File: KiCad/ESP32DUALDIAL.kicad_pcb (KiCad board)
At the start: 2 copper layers, 180.5 x 74 mm, 80 parts, among them J1 SERVICE, J2 Conn_01x04_Male, J3 mode, J5 Conn_01x03_Male, J6 Conn_01x02_Male, J7 Conn_01x02_Male, J8 Conn_01x02_Male, M1 Fan_CPU_4pin, M2 Fan_CPU_4pin, Q1 Q_NMOS_GDS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

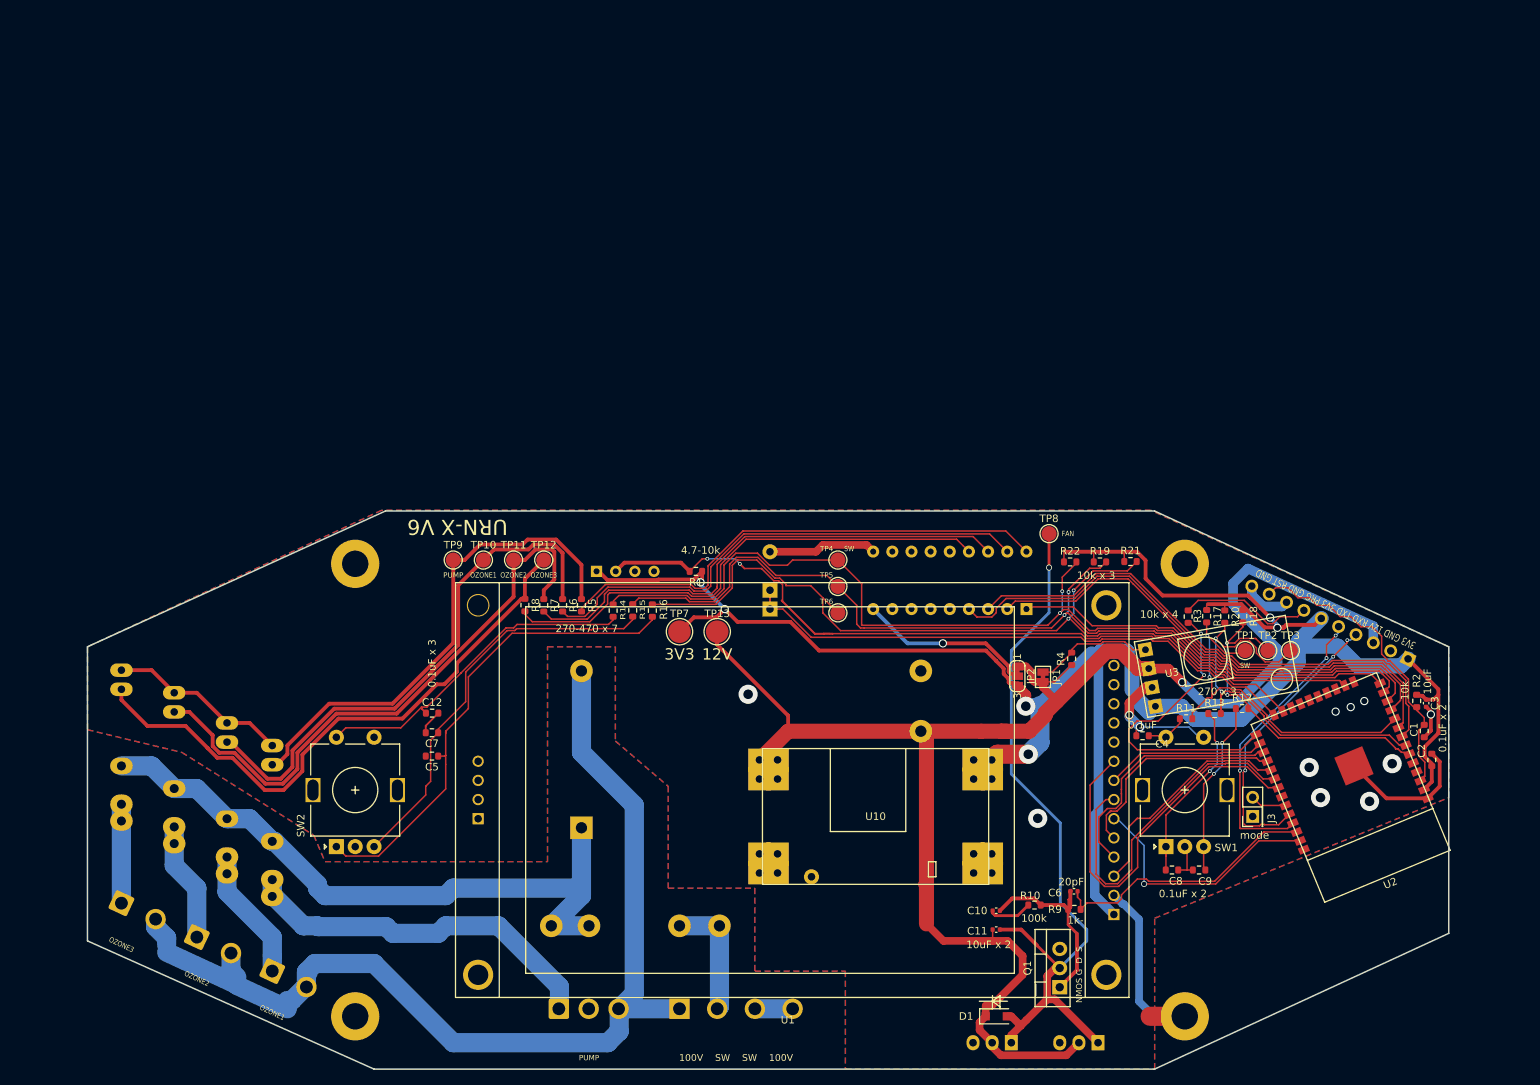
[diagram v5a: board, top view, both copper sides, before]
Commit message: Version6 release. Testpad add and follow more SSR type.
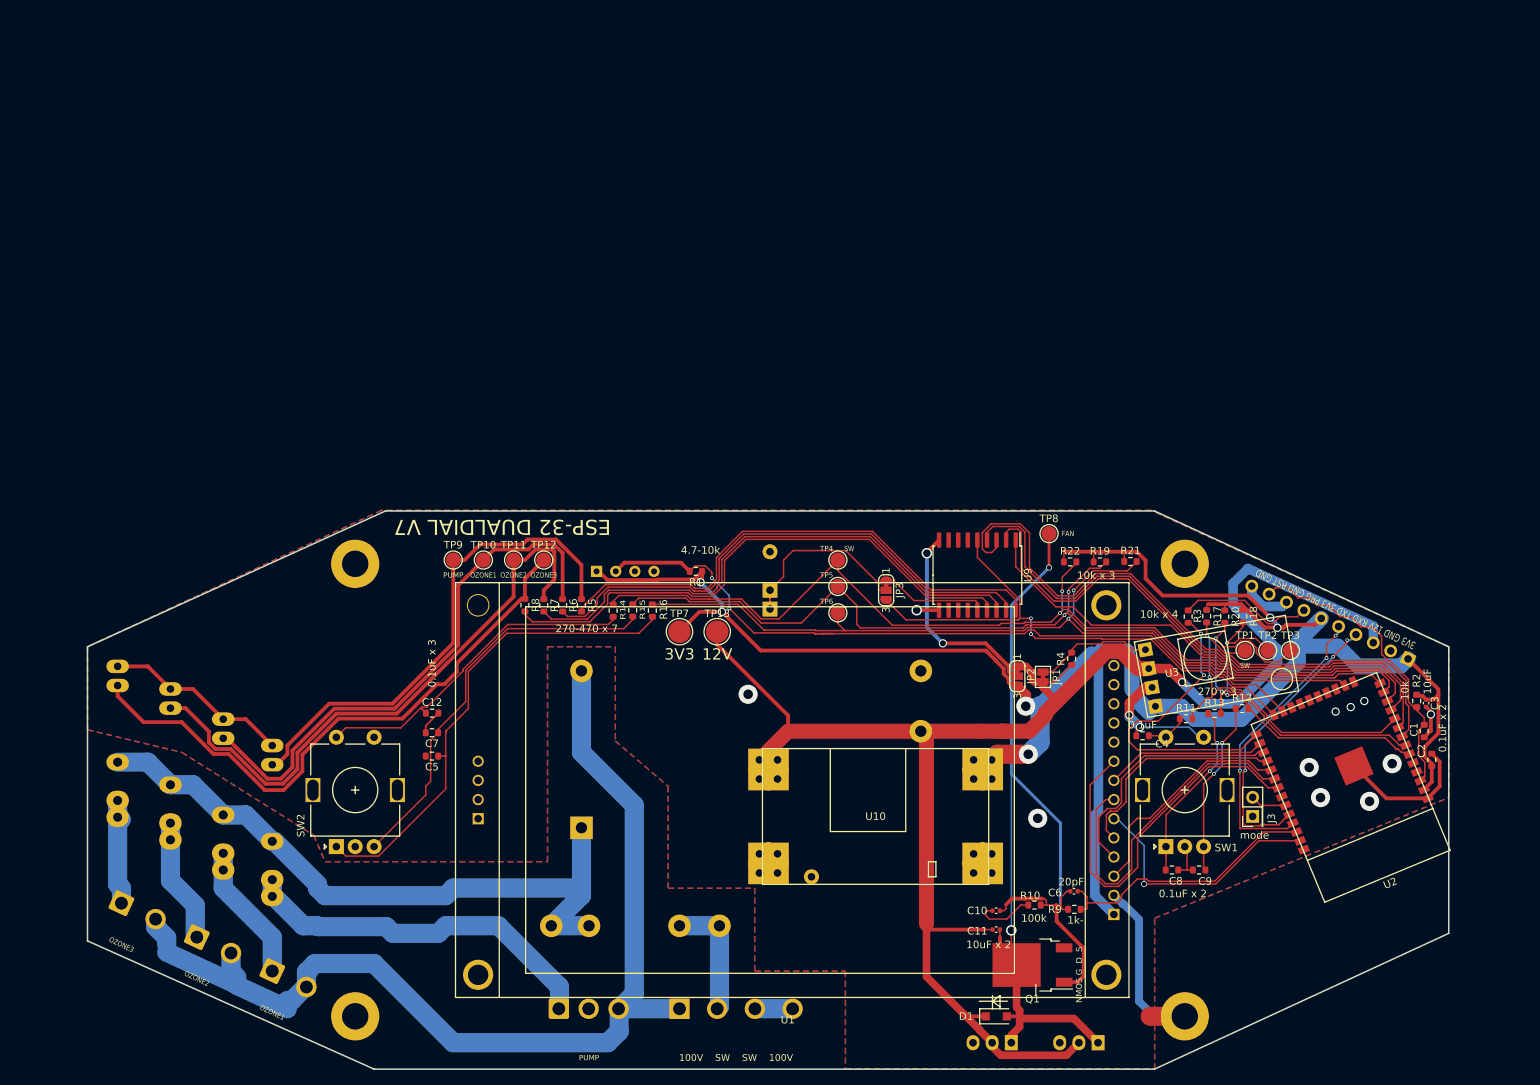
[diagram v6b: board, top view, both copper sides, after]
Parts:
- added JP3: Jumper_NC_Dual, Jumper:SolderJumper-3_P1.3mm_Bridged12_RoundedPad1.0x1.5mm_NumberLabels, F.Cu at (130.4, 83.5)
- Q1: footprint Package_TO_SOT_THT:TO-220-3_Vertical -> Package_TO_SOT_SMD:TO-252-2
- U9: footprint Package_DIP:DIP-18_W7.62mm -> Package_SO:SOIC-18W_7.5x11.6mm_P1.27mm; moved to F.Cu
- moved U9 7.91 mm to (142.5, 81.5), turned to 270 degrees
- moved Q1 4.66 mm to (149.8, 133.2), turned to 180 degrees
- moved U6 0.71 mm to (42.5, 109.5)
- moved U7 0.71 mm to (35.5, 105.5)
- moved U8 0.71 mm to (28.5, 102.5)
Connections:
- U2 pad 24: Net-(BZ1-Pad1) -> BUZZER
- U9 pad 5: Net-(U9-Pad5) -> BUZZER
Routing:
- net BUZZER: track 0.00 -> 72.1 mm, vias 0 -> 2
- net Net-(BZ1-Pad1): track 76.8 -> 25.5 mm
- net Net-(JP3-Pad1): track 0.00 -> 14.3 mm
- net OZON1: track 71.6 -> 84.3 mm
- net Net-(C11-Pad1): track 100.4 -> 108.9 mm, vias 1 -> 2
- net GND: track 128.6 -> 120.1 mm, vias 12 -> 13
- net Net-(R16-Pad2): track 122.5 -> 114.3 mm
- net OZON0: track 63.9 -> 71.6 mm
- net PUMP: track 56.5 -> 63.5 mm
- net Net-(R1-Pad2): track 108.8 -> 101.9 mm
- net Net-(R8-Pad2): track 67.8 -> 74.0 mm
- net Net-(R7-Pad2): track 67.6 -> 73.1 mm
- net Net-(JP2-Pad2): track 23.8 -> 27.9 mm, vias 1 -> 2
- net Net-(R6-Pad2): track 67.2 -> 71.0 mm
- net OZON2: track 73.0 -> 76.8 mm
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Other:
- board text added: "ESP-32 DUALDIAL V7"
- board text removed: "URN-X V6"

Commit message: arduino schtch update
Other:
- net class 220V removed
- net class 220VSub removed
- net class Default removed

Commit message: v8
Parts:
- removed JP1: Jumper, Jumper:SolderJumper-2_P1.3mm_Bridged_Pad1.0x1.5mm
- removed R4: NC, Resistor_SMD:R_0603_1608Metric
- removed U3: QS-1205CME-3A_MINIDC-DC_12-24Vto5V3A_1.8V_2.5V_3.3V_5V_9V_1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, library:QS-1205CME-3A_MINIDC-DC_12-24Vto5V3A_1.8V_2.5V_3.3V_5V_9V_12V
- added C13: 1000p, Capacitor_THT:C_Disc_D10.5mm_W5.0mm_P10.00mm, B.Cu at (123.6, 124.0)
- added C14: 1000p, Capacitor_THT:C_Disc_D10.5mm_W5.0mm_P10.00mm, B.Cu at (136.6, 124.0)
- added R23: 1MΩ, Resistor_THT:R_Axial_DIN0207_L6.3mm_D2.5mm_P10.16mm_Horizontal, B.Cu at (123.6, 129.8)
- added R24: 1MΩ, Resistor_THT:R_Axial_DIN0207_L6.3mm_D2.5mm_P10.16mm_Horizontal, B.Cu at (136.8, 129.8)
- U10: value Mini560_DC-DC_JW5068A -> ROAM BP5293-33; footprint library:Mini560_DC-DC_JW5068A -> Converter_DCDC:Converter_DCDC_RECOM_R-78E-0.5_THT
- moved U10 41.9 mm to (165.4, 92.7), turned to -90 degrees
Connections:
- BZ1 pad 2: GND -> Earth
- C1 pad 2: GND -> Earth
- C10 pad 1: GND -> Earth
- C12 pad 2: GND -> Earth
- C2 pad 2: GND -> Earth
- C3 pad 2: GND -> Earth
- C4 pad 2: GND -> Earth
- C5 pad 2: GND -> Earth
- C7 pad 2: GND -> Earth
- C8 pad 2: GND -> Earth
- C9 pad 2: GND -> Earth
- H1 pad 1: GND -> Earth
- H2 pad 1: GND -> Earth
- H3 pad 1: GND -> Earth
- H4 pad 1: GND -> Earth
- J1 pad 10: GND -> Earth
- J1 pad 2: GND -> Earth
- J1 pad 8: GND -> Earth
- J3 pad 1: GND -> Earth
- J5 pad 2: Net-(J5-Pad2) -> unconnected-(J5-Pin_2-Pad2)
- M1 pad 3: Net-(M1-Pad3) -> unconnected-(M1-Tacho-Pad3)
- M2 pad 3: Net-(M2-Pad3) -> unconnected-(M2-Tacho-Pad3)
- PS1 pad 3: GND -> Earth
- Q1 pad 3: GND -> Earth
- R10 pad 1: GND -> Earth
- SW1 pad C: GND -> Earth
- SW1 pad S1: GND -> Earth
- SW2 pad C: GND -> Earth
- SW2 pad S1: GND -> Earth
- U1 pad 10: Net-(U1-Pad10) -> unconnected-(U1-SD_CS-Pad10)
- U1 pad 11: Net-(U1-Pad11) -> unconnected-(U1-SD_MOSI-Pad11)
- U1 pad 12: Net-(U1-Pad12) -> unconnected-(U1-SD_MISO-Pad12)
- U1 pad 13: Net-(U1-Pad13) -> unconnected-(U1-SD_SCK-Pad13)
- U1 pad 14: Net-(U1-Pad14) -> unconnected-(U1-FLASH_CD-Pad14)
- U1 pad 2: GND -> Earth
- U10 pad 2: +3V3 -> Earth
- U10 pad 3: GND -> +3V3
- U2 pad 1: GND -> Earth
- U2 pad 15: GND -> Earth
- U2 pad 17: Net-(U2-Pad17) -> unconnected-(U2-SD2-Pad17)
- U2 pad 18: Net-(U2-Pad18) -> unconnected-(U2-SD3-Pad18)
- U2 pad 19: Net-(U2-Pad19) -> unconnected-(U2-CMD-Pad19)
- U2 pad 20: Net-(U2-Pad20) -> unconnected-(U2-CLK-Pad20)
- U2 pad 21: Net-(U2-Pad21) -> unconnected-(U2-SD0-Pad21)
- U2 pad 22: Net-(U2-Pad22) -> unconnected-(U2-SD1-Pad22)
- U2 pad 32: Net-(U2-Pad32) -> unconnected-(U2-NC-Pad32)
- U2 pad 38: GND -> Earth
- U2 pad 39: GND -> Earth
- U2 pad 4: Net-(U2-Pad4) -> unconnected-(U2-SENSOR_VP-Pad4)
- U2 pad 5: Net-(U2-Pad5) -> unconnected-(U2-SENSOR_VN-Pad5)
- U4 pad 3: Net-(U4-Pad3) -> unconnected-(U4-NC-Pad3)
- U4 pad 4: GND -> Earth
- U5 pad 4: GND -> Earth
- U6 pad 4: GND -> Earth
- U7 pad 4: GND -> Earth
- U8 pad 4: GND -> Earth
- U9 pad 10: GND -> Earth
- U9 pad 11: Net-(U9-Pad11) -> unconnected-(U9-O8-Pad11)
- U9 pad 12: Net-(U9-Pad12) -> unconnected-(U9-O7-Pad12)
- U9 pad 13: Net-(U9-Pad13) -> unconnected-(U9-O6-Pad13)
- U9 pad 6: Net-(U9-Pad6) -> unconnected-(U9-I6-Pad6)
- U9 pad 7: Net-(U9-Pad7) -> unconnected-(U9-I7-Pad7)
- U9 pad 8: Net-(U9-Pad8) -> unconnected-(U9-I8-Pad8)
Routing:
- net Earth: track 0.00 -> 211.0 mm, vias 0 -> 13
- net GND: track 120.1 -> 0.00 mm, vias 13 -> 0
- net Net-(J2-Pin_1): track 137.4 -> 185.0 mm
- net +12V: track 226.5 -> 199.3 mm
- net +3V3: track 301.4 -> 278.2 mm, vias 6 -> 5
- net Net-(JP1-Pad1): track 15.9 -> 0.00 mm
- net Net-(J2-Pin_2): track 16.4 -> 27.7 mm
- net Net-(BZ1--): track 25.5 -> 24.1 mm
- added copper zone on B.Cu, net Earth
- added copper zone on F.Cu, net Earth
- removed copper zone on B.Cu, net GND
- removed copper zone on F.Cu, net GND
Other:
- board text added: "ESP-32 DUALDIAL V8"
- board text removed: "ESP-32 DUALDIAL V7"
